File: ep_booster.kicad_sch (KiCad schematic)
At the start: 28 parts, among them J2 Screw_Terminal_01x04, Q1 J201, Q2 2N5088, SW1 SW_SPDT, SW2 SW_SPDT

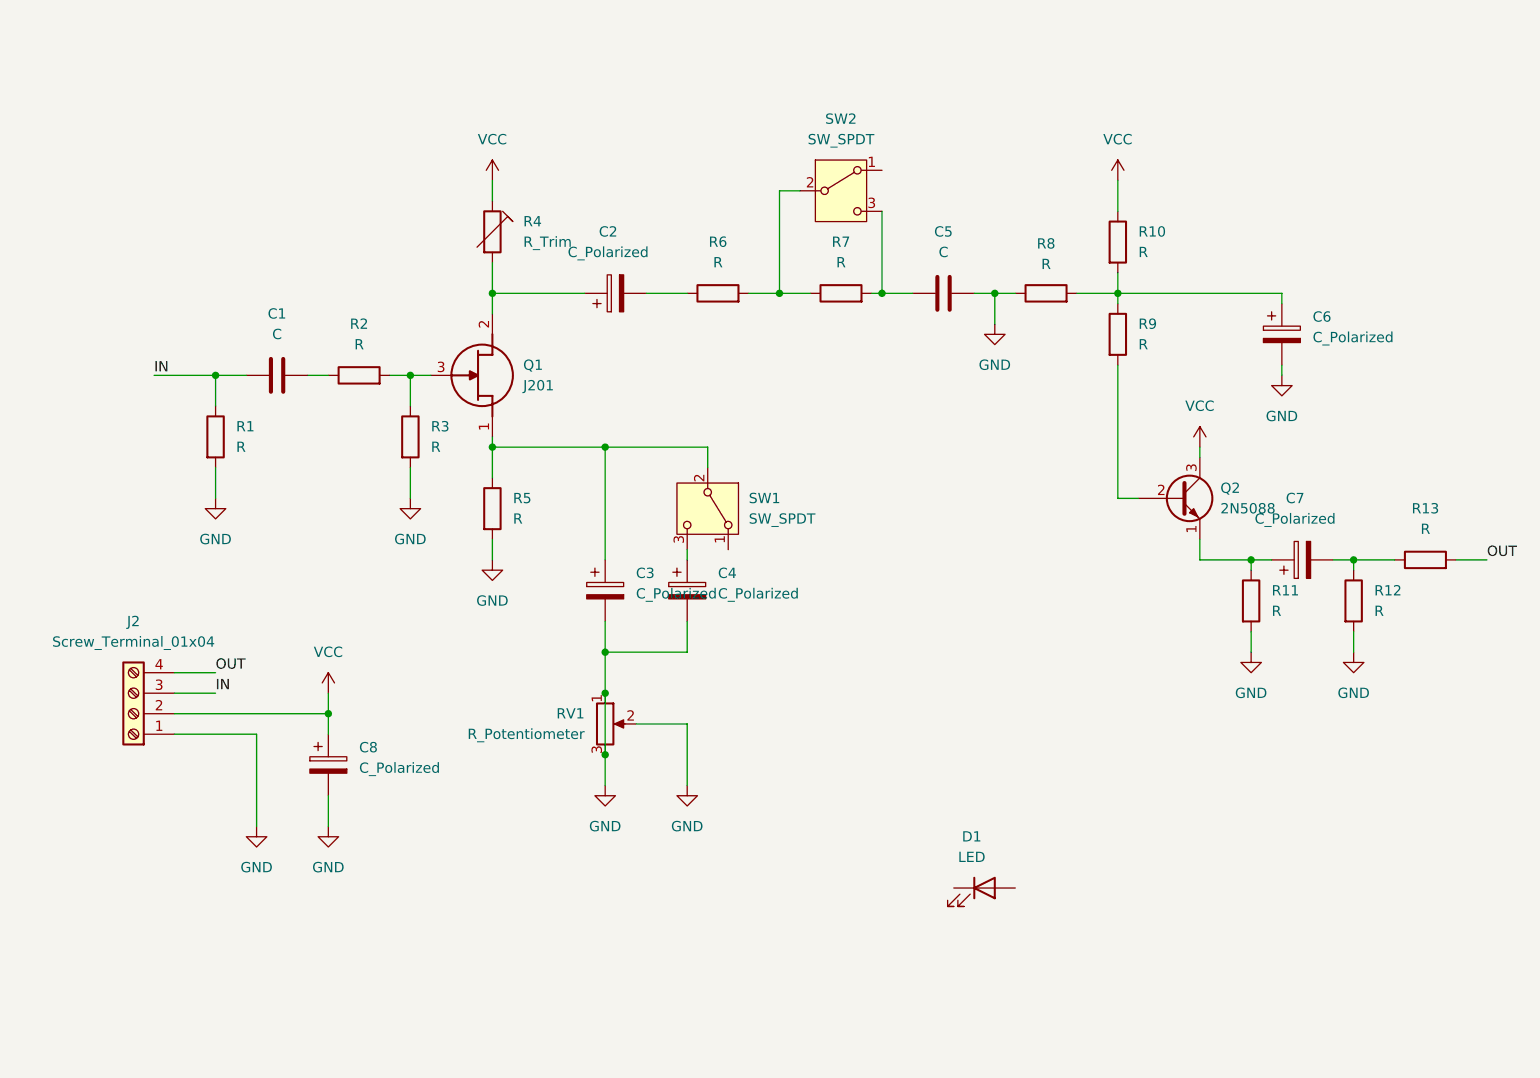
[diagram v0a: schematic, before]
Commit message: traced board from aionfx
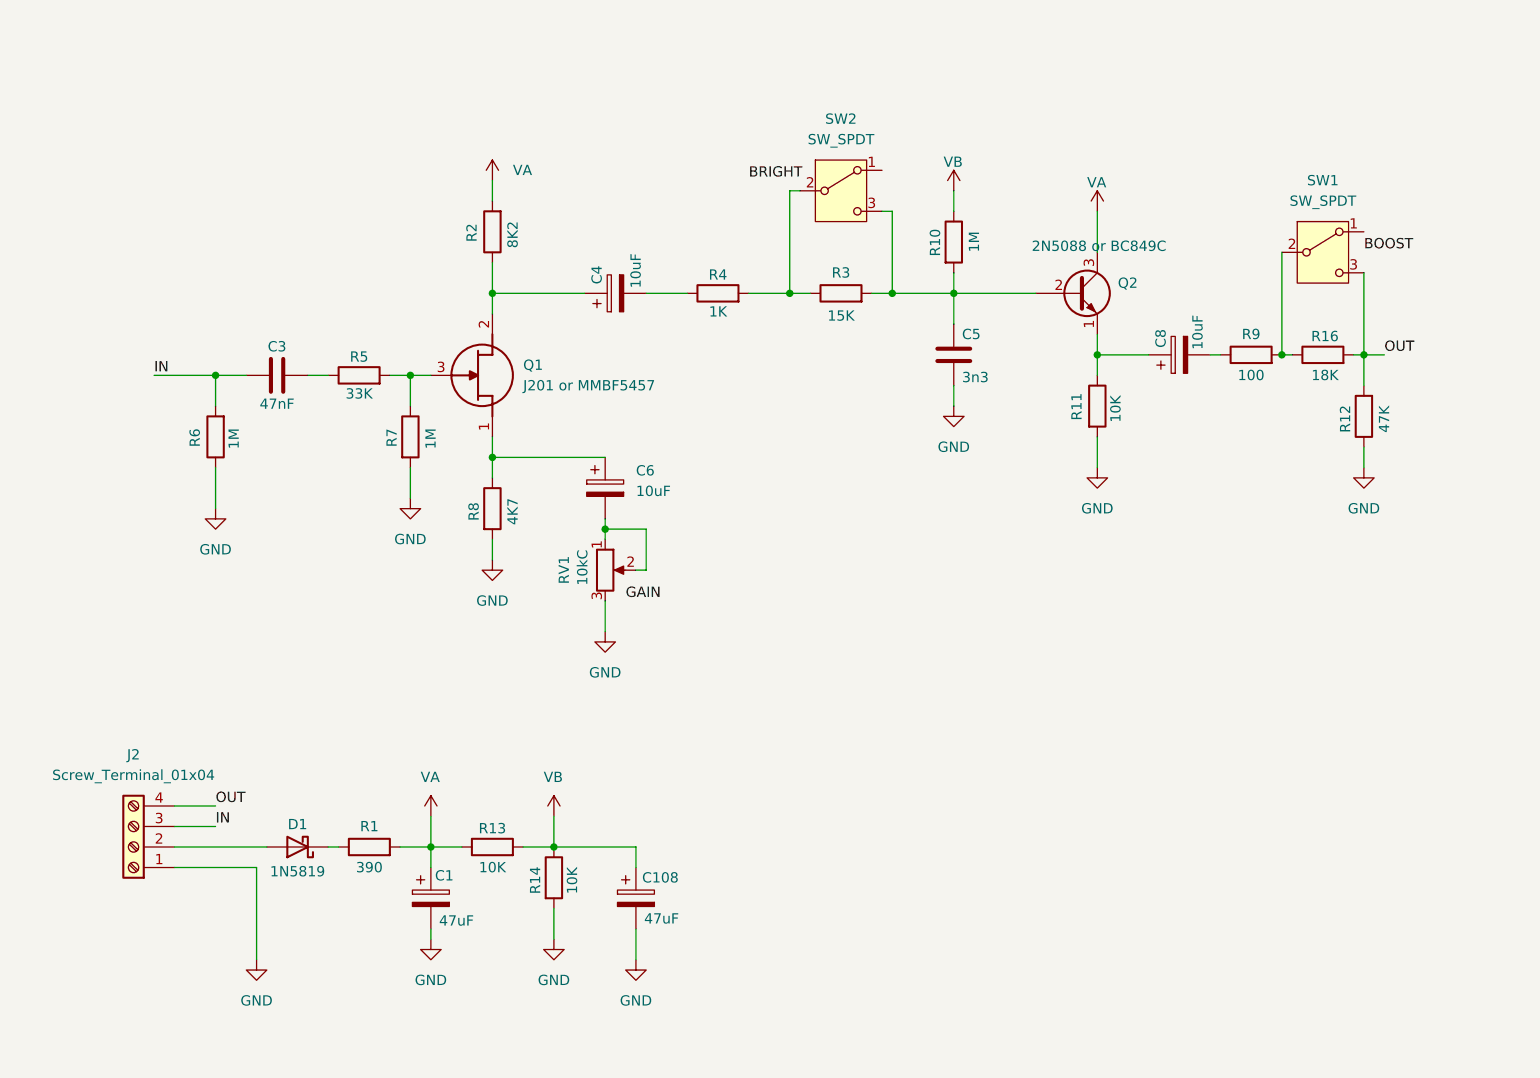
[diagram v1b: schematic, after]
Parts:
- removed C4: C_Polarized, symbol Device:C_Polarized
- removed C5: C, symbol Device:C
- removed D1: LED, symbol Device:LED
- removed R4: R_Trim, symbol Device:R_Trim
- removed R8: R, symbol Device:R
- added C1: 47uF, symbol Device:C_Polarized
- added D1: 1N5819, symbol Device:D_Schottky
- added R13, R14: 10K, symbol Device:R
- added R2: 8K2, symbol Device:R
- added R6: 1M, symbol Device:R
- C108: renamed from C8; value C_Polarized -> 47uF
- C3: renamed from C1; value C -> 47nF
- C4: renamed from C2; value C_Polarized -> 10uF
- C5: renamed from C6; value C_Polarized -> 3n3; symbol Device:C_Polarized -> Device:C
- C6: renamed from C3; value C_Polarized -> 10uF
- C8: renamed from C7; value C_Polarized -> 10uF
- Q1: value J201 -> J201 or MMBF5457
- Q2: value 2N5088 -> 2N5088 or BC849C
- R1: value R -> 390
- R10: value R -> 1M
- R11: value R -> 10K
- R12: value R -> 47K
- R16: renamed from R13; value R -> 18K
- R3: renamed from R7; value R -> 15K
- R4: renamed from R6; value R -> 1K
- R5: renamed from R2; value R -> 33K
- R7: renamed from R3; value R -> 1M
- R8: renamed from R5; value R -> 4K7
- R9: value R -> 100
- RV1: value R_Potentiometer -> 10kC
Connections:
- net GND: now also R12.1, C1.2, R14.2, R6.1; no longer C6.2, R1.2, R12.2, RV1.1, RV1.2
- net IN: now also R6.2; no longer R1.1
- net OUT: now also R12.2, SW1.3 (C)
- net at C5.1, R10.2: now also Q2.2 (B), R3.2, SW2.3 (C); no longer R9.1
- net at C6.1, Q1.1 (S), R8.1: no longer SW1.2 (B)
- net at C4.1, Q1.2 (D): now also R2.1
- net at R9.2: now also R16.1, SW1.2 (B); no longer Q2.2 (B)
- net VCC renamed VB
- net VB: now also R13.2, R14.1; no longer J2.2 (Pin_2), Q2.3 (C)
- new net: C8.2, R9.1
- new net: D1.1 (K), R1.1
- new net: D1.2 (A), J2.2 (Pin_2)
- new net: C6.2, RV1.1, RV1.2
- new net VA: C1.1, Q2.3 (C), R1.2, R13.1, R2.2
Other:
- moved on the sheet: C108, C6, C8, J2, Q2, R10, R11, R16, RV1

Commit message: footprint association
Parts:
- C3, C5: footprint (none) -> Capacitor_THT:C_Rect_L13.0mm_W6.0mm_P10.00mm_FKS3_FKP3_MKS4
- D1: footprint (none) -> Diode_THT:D_DO-41_SOD81_P7.62mm_Horizontal
- R1, R10, R11, R12, R13, R14, R16, R2, R3, R4, R5, R6, R7, R8, R9: footprint (none) -> Resistor_THT:R_Axial_DIN0204_L3.6mm_D1.6mm_P7.62mm_Horizontal
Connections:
- no-connect marks 0 -> 2
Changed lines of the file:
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@@
 		(color 0 0 0 0)
 	)
+	(no_connect
+		(at 116.84 29.21)
+	)
+	(no_connect
+		(at 176.53 36.83)
+	)
 	(wire
 		(pts
@@
 		)
 	)
-	(label "GAIN"
-		(at 85.09 82.55 0)
-		(fields_autoplaced yes)
-		(effects
-			(font
-				(size 1.27 1.27)
-			)
-			(justify left bottom)
-		)
-	)
-	(label "BOOST"
-		(at 176.53 39.37 0)
-		(fields_autoplaced yes)
-		(effects
-			(font
-				(size 1.27 1.27)
-			)
-			(justify left bottom)
-		)
-	)
-	(label "BRIGHT"
-		(at 100.33 30.48 0)
-		(fields_autoplaced yes)
-		(effects
-			(font
-				(size 1.27 1.27)
-			)
-			(justify left bottom)
-		)
-	)
 	(label "OUT"
 		(at 34.29 107.95 0)
@@
 			)
 		)
-		(property "Footprint" ""
+		(property "Footprint" "Resistor_THT:R_Axial_DIN0204_L3.6mm_D1.6mm_P7.62mm_Horizontal"
 			(at 56.642 62.23 90)
 			(effects
@@
 			)
 		)
-		(property "Footprint" ""
+		(property "Footprint" "Resistor_THT:R_Axial_DIN0204_L3.6mm_D1.6mm_P7.62mm_Horizontal"
 			(at 123.952 38.1 90)
 			(effects
@@
 			)
 		)
-		(property "Footprint" ""
+		(property "Footprint" "Resistor_THT:R_Axial_DIN0204_L3.6mm_D1.6mm_P7.62mm_Horizontal"
 			(at 162.56 53.848 90)
 			(effects
@@
 			)
 		)
-		(property "Footprint" ""
+		(property "Footprint" "Capacitor_THT:C_Rect_L13.0mm_W6.0mm_P10.00mm_FKS3_FKP3_MKS4"
 			(at 45.72 53.6448 0)
 			(effects
@@
 			)
 		)
-		(property "Footprint" ""
+		(property "Footprint" "Diode_THT:D_DO-41_SOD81_P7.62mm_Horizontal"
 			(at 44.45 113.03 0)
 			(effects
@@
 			)
 		)
-		(property "Footprint" ""
+		(property "Footprint" "Resistor_THT:R_Axial_DIN0204_L3.6mm_D1.6mm_P7.62mm_Horizontal"
 			(at 111.76 46.228 90)
 			(effects
@@
 			)
 		)
-		(property "Footprint" ""
+		(property "Footprint" "Resistor_THT:R_Axial_DIN0204_L3.6mm_D1.6mm_P7.62mm_Horizontal"
 			(at 141.732 58.42 90)
 			(effects
@@
 			)
 		)
-		(property "Footprint" ""
+		(property "Footprint" "Resistor_THT:R_Axial_DIN0204_L3.6mm_D1.6mm_P7.62mm_Horizontal"
 			(at 68.58 114.808 90)
 			(effects
@@
 			)
 		)
-		(property "Footprint" ""
+		(property "Footprint" "Resistor_THT:R_Axial_DIN0204_L3.6mm_D1.6mm_P7.62mm_Horizontal"
 			(at 70.358 36.83 90)
 			(effects
@@
 			)
 		)
-		(property "Footprint" ""
+		(property "Footprint" "Capacitor_THT:C_Rect_L13.0mm_W6.0mm_P10.00mm_FKS3_FKP3_MKS4"
 			(at 126.6952 55.88 0)
 			(effects
@@
 			)
 		)
-		(property "Footprint" ""
+		(property "Footprint" "Resistor_THT:R_Axial_DIN0204_L3.6mm_D1.6mm_P7.62mm_Horizontal"
 			(at 96.52 46.228 90)
 			(effects
@@
 			)
 		)
-		(property "Footprint" ""
+		(property "Footprint" "Resistor_THT:R_Axial_DIN0204_L3.6mm_D1.6mm_P7.62mm_Horizontal"
 			(at 53.34 114.808 90)
 			(effects
@@
 			)
 		)
-		(property "Footprint" ""
+		(property "Footprint" "Resistor_THT:R_Axial_DIN0204_L3.6mm_D1.6mm_P7.62mm_Horizontal"
 			(at 178.308 59.69 90)
 			(effects
@@
 			)
 		)
-		(property "Footprint" ""
+		(property "Footprint" "Resistor_THT:R_Axial_DIN0204_L3.6mm_D1.6mm_P7.62mm_Horizontal"
 			(at 171.45 53.848 90)
 			(effects
@@
 			)
 		)
-		(property "Footprint" ""
+		(property "Footprint" "Resistor_THT:R_Axial_DIN0204_L3.6mm_D1.6mm_P7.62mm_Horizontal"
 			(at 66.802 71.12 90)
 			(effects
@@
 			)
 		)
-		(property "Footprint" ""
+		(property "Footprint" "Resistor_THT:R_Axial_DIN0204_L3.6mm_D1.6mm_P7.62mm_Horizontal"
 			(at 52.07 56.388 90)
 			(effects
@@
 			)
 		)
-		(property "Footprint" ""
+		(property "Footprint" "Resistor_THT:R_Axial_DIN0204_L3.6mm_D1.6mm_P7.62mm_Horizontal"
 			(at 36.068 62.23 90)
 			(effects
@@
 			)
 		)
-		(property "Footprint" ""
+		(property "Footprint" "Resistor_THT:R_Axial_DIN0204_L3.6mm_D1.6mm_P7.62mm_Horizontal"
 			(at 74.422 116.84 90)
 			(effects

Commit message: libs and pcb design update
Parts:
- removed J2: Screw_Terminal_01x04, TerminalBlock:TerminalBlock_Xinya_XY308-2.54-4P_1x04_P2.54mm_Horizontal, symbol Connector:Screw_Terminal_01x04
- removed Q1: J201 or MMBF5457, PN4117, symbol J201:J201
- removed Q2: 2N5088 or BC849C, Package_TO_SOT_THT:TO-18-3, symbol Transistor_BJT:BC107
- removed SW1, SW2: SW_SPDT, symbol Switch:SW_SPDT
- added J1: TB002-500-04BE, footprints:TB00250004BE, symbol TB002-500-04BE:TB002-500-04BE
- added Q1: MMBF5457, Package_TO_SOT_SMD:SOT-23, symbol Transistor_FET:BF545B
- added Q2: BC849C, Package_TO_SOT_SMD:SOT-23, symbol Transistor_BJT:SS8050
- added SW1: SW_DIP_x02, DS03-254-02BE:DS0325402BE, symbol Switch:SW_DIP_x02
- C1, C108: footprint (none) -> Capacitor_THT:CP_Radial_D6.3mm_P2.50mm
- C3, C5: footprint Capacitor_THT:C_Rect_L13.0mm_W6.0mm_P10.00mm_FKS3_FKP3_MKS4 -> Capacitor_THT:C_Rect_L7.2mm_W2.5mm_P5.00mm_FKS2_FKP2_MKS2_MKP2
- C4, C6, C8: footprint (none) -> Capacitor_THT:CP_Radial_D5.0mm_P2.50mm
- R1, R10, R11, R12, R13, R14, R16, R2, R3, R4, R5, R6, R7, R8, R9: footprint Resistor_THT:R_Axial_DIN0204_L3.6mm_D1.6mm_P7.62mm_Horizontal -> Resistor_SMD:R_1206_3216Metric_Pad1.30x1.75mm_HandSolder
- RV1: footprint (none) -> milos.garunovic:mg_3306K1103
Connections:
- net GND: now also J1.1
- net IN: now also J1.3
- net OUT: now also J1.4, SW1.3
- net VA: now also Q2.3 (C)
- net at R5.2, R7.1: now also Q1.3 (G)
- net at C5.1, R10.2, R3.2: now also Q2.1 (B), SW1.4
- net at R16.1, R9.2: now also SW1.2
- net at C8.1, R11.1: now also Q2.2 (E)
- net at D1.2 (A): now also J1.2
- net at C6.1, R8.1: now also Q1.1 (S)
- net at C4.1, R2.1: now also Q1.2 (D)
- net at R3.1, R4.2: now also SW1.1
- no-connect marks 2 -> 0

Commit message: libs and pcb design update (2)
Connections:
- net GND: now also J1.4; no longer J1.1
- net IN: now also J1.1; no longer J1.3
- net OUT: now also J1.2; no longer J1.4
- net at D1.2 (A): now also J1.3; no longer J1.2
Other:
- moved on the sheet: C1, C108, D1, R1, R13, R14
